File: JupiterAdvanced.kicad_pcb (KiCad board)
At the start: 2 copper layers, 314.8 x 162.9 mm, 224 parts, among them SW1 SW_Push, U1 PRTR5V0U2X, U10 ATmega32U4-AU, Y1 16MHz

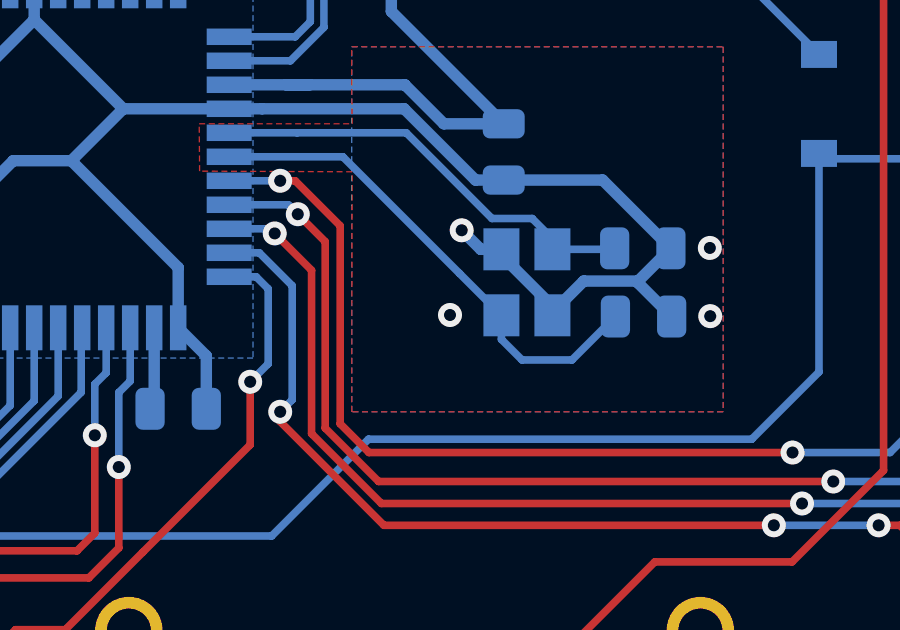
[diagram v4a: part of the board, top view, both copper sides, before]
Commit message: removed surplus via
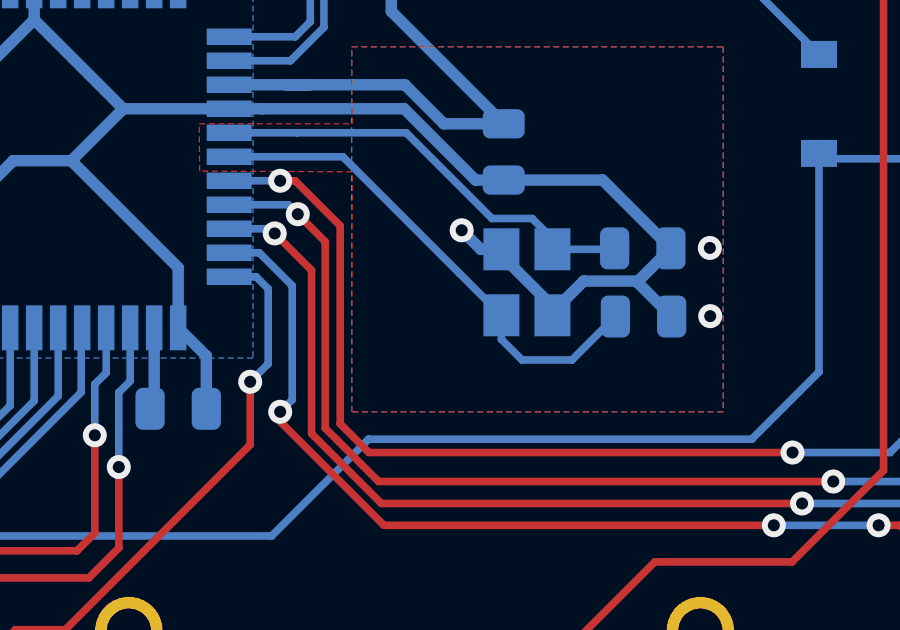
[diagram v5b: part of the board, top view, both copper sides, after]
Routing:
- net Net-(R7-Pad2): vias 1 -> 0
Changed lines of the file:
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@@
     (thickness 1.6)
     (drawings 547)
-    (tracks 996)
+    (tracks 995)
     (zones 0)
     (modules 224)
@@
   (segment (start 268.8625 98.905632) (end 265.725 102.043132) (width 0.254) (layer B.Cu) (net 139))
   (segment (start 268.8625 97.075) (end 268.8625 98.905632) (width 0.254) (layer B.Cu) (net 139))
-  (via (at 278.78532 113.74882) (size 0.8) (drill 0.4) (layers F.Cu B.Cu) (net 140))
   (segment (start 261.725 116.375) (end 261.325 116.775) (width 0.254) (layer B.Cu) (net 140))
   (segment (start 261.725 114.175) (end 261.725 116.375) (width 0.254) (layer B.Cu) (net 140))

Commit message: Rerouting for atmega32u4 complete
and its a complete mess...
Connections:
- U10 pad 10: ROW5 -> ROW6
- U10 pad 11: ROW6 -> ROW0
- U10 pad 9: ROW0 -> ROW5
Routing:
- net ROW5: track 586.8 -> 869.1 mm, vias 0 -> 2
- net ROW6: track 698.7 -> 832.7 mm, vias 0 -> 3
- net ROW0: track 517.7 -> 595.9 mm, vias 3 -> 8

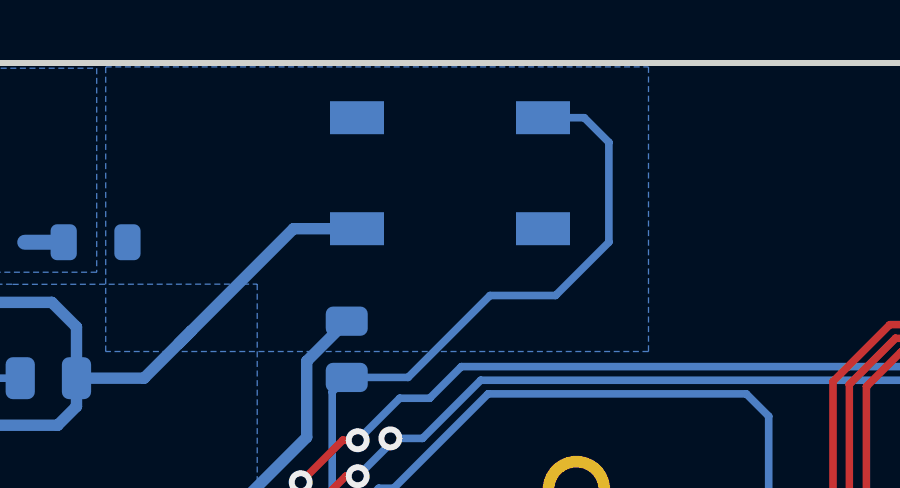
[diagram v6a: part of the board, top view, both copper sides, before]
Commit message: Push switch updated for JLCPCB
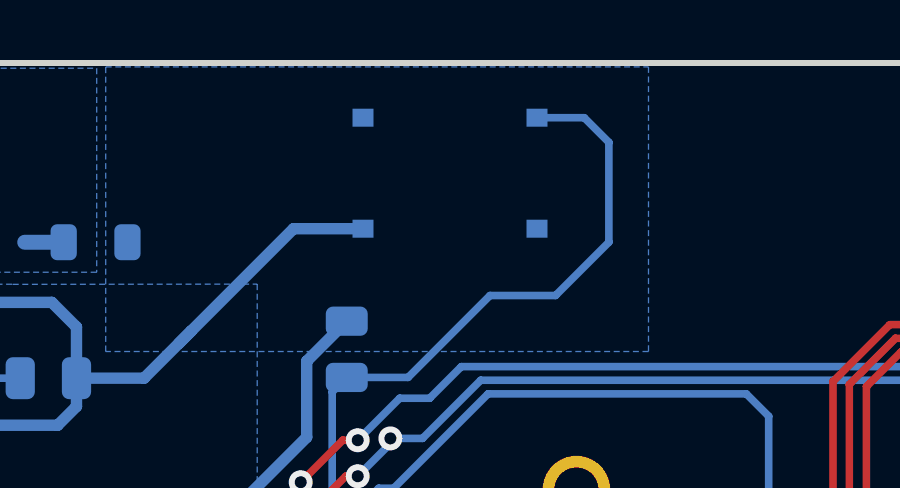
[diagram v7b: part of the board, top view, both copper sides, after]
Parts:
- SW1: footprint random-keyboard-parts:SKQG-1155865 -> JupiterAdvancedKbd_localFP:TS-1187A-B-A-B
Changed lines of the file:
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@@
     (add_net VCC)
+  )
+  (module JupiterAdvancedKbd_localFP:TS-1187A-B-A-B (layer B.Cu)
+    (at 283.00172 85.17382 180)
+    (fp_text reference SW1 (at 0.02794 3.556) (layer B.SilkS)
+      (effects (font (size 1 1) (thickness 0.15)) (justify mirror))
+    )
+    (fp_text value SW_Push (at -0.0254 -3.45948) (layer B.Fab)
+      (effects (font (size 1 1) (thickness 0.15)) (justify mirror))
+    )
+    (fp_line (start 3.25 2.15) (end 3.25 -2.15) (layer B.Fab) (width 0.12))
+    (fp_line (start -3.25 2.15) (end -3.25 -2.15) (layer B.Fab) (width 0.12))
+    (fp_line (start -3.25 -2.15) (end 3.25 -2.15) (layer B.Fab) (width 0.12))
+    (fp_line (start -3.25 2.15) (end 3.25 2.15) (layer B.Fab) (width 0.12))
+    (fp_line (start -3.2512 2.15392) (end -3.2512 -2.14608) (layer B.SilkS) (width 0.2))
+    (fp_line (start -3.2512 -2.15) (end 3.2488 -2.15) (layer B.SilkS) (width 0.2))
+    (fp_line (start 3.24612 2.15392) (end 3.24612 -2.14608) (layer B.SilkS) (width 0.2))
+    (fp_line (start -3.25388 2.15392) (end 3.24612 2.15392) (layer B.SilkS) (width 0.2))
+    (pad 1 smd rect (at -2.9 1.85 180) (size 0.7 0.6) (layers B.Cu B.Paste B.Mask)
+      (net 9 GND))
+    (pad 2 smd rect (at 2.9 1.85 180) (size 0.7 0.6) (layers B.Cu B.Paste B.Mask)
+      (net 131 "Net-(R8-Pad2)"))
+    (pad 3 smd rect (at -2.9 -1.85 180) (size 0.7 0.6) (layers B.Cu B.Paste B.Mask))
+    (pad 4 smd rect (at 2.9 -1.85 180) (size 0.7 0.6) (layers B.Cu B.Paste B.Mask))
   )
   (module Package_QFP:TQFP-44_10x10mm_P0.8mm (layer B.Cu)
@@
     (pad "" np_thru_hole circle (at 5.08 0 48.0996) (size 1.75 1.75) (drill 1.75) (layers *.Cu *.Mask))
   )
-  (module random-keyboard-parts:SKQG-1155865 (layer B.Cu)
-    (at 283.00172 85.17382 180)
-    (attr smd)
-    (fp_text reference SW1 (at 0 -4.064) (layer B.SilkS)
-      (effects (font (size 1 1) (thickness 0.15)) (justify mirror))
-    )
-    (fp_text value SW_Push (at 0 4.064) (layer B.Fab)
-      (effects (font (size 1 1) (thickness 0.15)) (justify mirror))
-    )
-    (fp_line (start -2.6 2.6) (end 2.6 2.6) (layer B.SilkS) (width 0.15))
-    (fp_line (start 2.6 2.6) (end 2.6 -2.6) (layer B.SilkS) (width 0.15))
-    (fp_line (start 2.6 -2.6) (end -2.6 -2.6) (layer B.SilkS) (width 0.15))
-    (fp_line (start -2.6 -2.6) (end -2.6 2.6) (layer B.SilkS) (width 0.15))
-    (fp_circle (center 0 0) (end 1 0) (layer B.SilkS) (width 0.15))
-    (fp_line (start -4.2 2.6) (end 4.2 2.6) (layer B.Fab) (width 0.15))
-    (fp_line (start 4.2 2.6) (end 4.2 1.2) (layer B.Fab) (width 0.15))
-    (fp_line (start 4.2 1.1) (end 2.6 1.1) (layer B.Fab) (width 0.15))
-    (fp_line (start 2.6 1.1) (end 2.6 -1.1) (layer B.Fab) (width 0.15))
-    (fp_line (start 2.6 -1.1) (end 4.2 -1.1) (layer B.Fab) (width 0.15))
-    (fp_line (start 4.2 -1.1) (end 4.2 -2.6) (layer B.Fab) (width 0.15))
-    (fp_line (start 4.2 -2.6) (end -4.2 -2.6) (layer B.Fab) (width 0.15))
-    (fp_line (start -4.2 -2.6) (end -4.2 -1.1) (layer B.Fab) (width 0.15))
-    (fp_line (start -4.2 -1.1) (end -2.6 -1.1) (layer B.Fab) (width 0.15))
-    (fp_line (start -2.6 -1.1) (end -2.6 1.1) (layer B.Fab) (width 0.15))
-    (fp_line (start -2.6 1.1) (end -4.2 1.1) (layer B.Fab) (width 0.15))
-    (fp_line (start -4.2 1.1) (end -4.2 2.6) (layer B.Fab) (width 0.15))
-    (fp_circle (center 0 0) (end 1 0) (layer B.Fab) (width 0.15))
-    (fp_line (start -2.6 1.1) (end -1.1 2.6) (layer B.Fab) (width 0.15))
-    (fp_line (start 2.6 1.1) (end 1.1 2.6) (layer B.Fab) (width 0.15))
-    (fp_line (start 2.6 -1.1) (end 1.1 -2.6) (layer B.Fab) (width 0.15))
-    (fp_line (start -2.6 -1.1) (end -1.1 -2.6) (layer B.Fab) (width 0.15))
-    (pad 4 smd rect (at -3.1 -1.85 180) (size 1.8 1.1) (layers B.Cu B.Paste B.Mask))
-    (pad 3 smd rect (at 3.1 1.85 180) (size 1.8 1.1) (layers B.Cu B.Paste B.Mask))
-    (pad 2 smd rect (at -3.1 1.85 180) (size 1.8 1.1) (layers B.Cu B.Paste B.Mask)
-      (net 131 "Net-(R8-Pad2)"))
-    (pad 1 smd rect (at 3.1 -1.85 180) (size 1.8 1.1) (layers B.Cu B.Paste B.Mask)
-      (net 9 GND))
-    (model ${KISYS3DMOD}/Button_Switch_SMD.3dshapes/SW_SPST_TL3342.step
-      (at (xyz 0 0 0))
-      (scale (xyz 1 1 1))
-      (rotate (xyz 0 0 0))
-    )
-  )
   (module MX_Only:MXOnly-6.25U-NoLED (layer F.Cu)

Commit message: JLCPCB Order SMT0210420181311
SMT0210420181311-3234210A
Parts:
- FB1: footprint Inductor_SMD:L_0805_2012Metric -> Inductor_SMD:L_1206_3216Metric
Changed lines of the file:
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@@
       (psa4output false)
       (plotreference true)
-      (plotvalue true)
+      (plotvalue false)
       (plotinvisibletext false)
       (padsonsilk false)
-      (subtractmaskfromsilk false)
+      (subtractmaskfromsilk true)
       (outputformat 1)
       (mirror false)
       (drillshape 0)
       (scaleselection 1)
-      (outputdirectory "Gerber/"))
+      (outputdirectory "JLCPCB/"))
   )
   (net 0 "")
@@
     (pad 4 smd rect (at 2.9 -1.85 180) (size 0.7 0.6) (layers B.Cu B.Paste B.Mask))
   )
+  (module Inductor_SMD:L_1206_3216Metric (layer B.Cu)
+    (at 271.1875 87.475 180)
+    (descr "Inductor SMD 1206 (3216 Metric), square (rectangular) end terminal, IPC_7351 nominal, (Body size source: IPC-SM-782 page 80, https://www.pcb-3d.com/wordpress/wp-content/uploads/ipc-sm-782a_amendment_1_and_2.pdf), generated with kicad-footprint-generator")
+    (tags inductor)
+    (attr smd)
+    (fp_text reference FB1 (at 0 1.9) (layer B.SilkS)
+      (effects (font (size 1 1) (thickness 0.15)) (justify mirror))
+    )
+    (fp_text value 60@100MHz (at 0 -1.9) (layer B.Fab)
+      (effects (font (size 1 1) (thickness 0.15)) (justify mirror))
+    )
+    (fp_text user %R (at 0 0) (layer B.Fab)
+      (effects (font (size 0.8 0.8) (thickness 0.12)) (justify mirror))
+    )
+    (fp_line (start -1.6 -0.8) (end -1.6 0.8) (layer B.Fab) (width 0.1))
+    (fp_line (start -1.6 0.8) (end 1.6 0.8) (layer B.Fab) (width 0.1))
+    (fp_line (start 1.6 0.8) (end 1.6 -0.8) (layer B.Fab) (width 0.1))
+    (fp_line (start 1.6 -0.8) (end -1.6 -0.8) (layer B.Fab) (width 0.1))
+    (fp_line (start -0.835242 0.91) (end 0.835242 0.91) (layer B.SilkS) (width 0.12))
+    (fp_line (start -0.835242 -0.91) (end 0.835242 -0.91) (layer B.SilkS) (width 0.12))
+    (fp_line (start -2.35 -1.2) (end -2.35 1.2) (layer B.CrtYd) (width 0.05))
+    (fp_line (start -2.35 1.2) (end 2.35 1.2) (layer B.CrtYd) (width 0.05))
+    (fp_line (start 2.35 1.2) (end 2.35 -1.2) (layer B.CrtYd) (width 0.05))
+    (fp_line (start 2.35 -1.2) (end -2.35 -1.2) (layer B.CrtYd) (width 0.05))
+    (pad 2 smd roundrect (at 1.575 0 180) (size 1.05 1.9) (layers B.Cu B.Paste B.Mask) (roundrect_rratio 0.2380942857142857)
+      (net 136 Earth))
+    (pad 1 smd roundrect (at -1.575 0 180) (size 1.05 1.9) (layers B.Cu B.Paste B.Mask) (roundrect_rratio 0.2380942857142857)
+      (net 9 GND))
+    (model ${KISYS3DMOD}/Inductor_SMD.3dshapes/L_1206_3216Metric.wrl
+      (at (xyz 0 0 0))
+      (scale (xyz 1 1 1))
+      (rotate (xyz 0 0 0))
+    )
+  )
   (module Package_QFP:TQFP-44_10x10mm_P0.8mm (layer B.Cu)
     (at 265.725 108.475 270)
@@
       (at (xyz 0 0 0))
       (scale (xyz 1 1 1))
-      (rotate (xyz 0 0 0))
-    )
-  )
-  (module Inductor_SMD:L_0805_2012Metric (layer B.Cu)
-    (at 271.1875 87.475 180)
-    (descr "Inductor SMD 0805 (2012 Metric), square (rectangular) end terminal, IPC_7351 nominal, (Body size source: IPC-SM-782 page 80, https://www.pcb-3d.com/wordpress/wp-content/uploads/ipc-sm-782a_amendment_1_and_2.pdf), generated with kicad-footprint-generator")
-    (tags inductor)
-    (attr smd)
-    (fp_text reference FB1 (at 0 1.55) (layer B.SilkS)
-      (effects (font (size 1 1) (thickness 0.15)) (justify mirror))
-    )
-    (fp_text value 60@100MHz (at 0 -1.55) (layer B.Fab)
-      (effects (font (size 1 1) (thickness 0.15)) (justify mirror))
-    )
-    (fp_line (start -1 -0.45) (end -1 0.45) (layer B.Fab) (width 0.1))
-    (fp_line (start -1 0.45) (end 1 0.45) (layer B.Fab) (width 0.1))
-    (fp_line (start 1 0.45) (end 1 -0.45) (layer B.Fab) (width 0.1))
-    (fp_line (start 1 -0.45) (end -1 -0.45) (layer B.Fab) (width 0.1))
-    (fp_line (start -0.399622 0.56) (end 0.399622 0.56) (layer B.SilkS) (width 0.12))
-    (fp_line (start -0.399622 -0.56) (end 0.399622 -0.56) (layer B.SilkS) (width 0.12))
-    (fp_line (start -1.75 -0.85) (end -1.75 0.85) (layer B.CrtYd) (width 0.05))
-    (fp_line (start -1.75 0.85) (end 1.75 0.85) (layer B.CrtYd) (width 0.05))
-    (fp_line (start 1.75 0.85) (end 1.75 -0.85) (layer B.CrtYd) (width 0.05))
-    (fp_line (start 1.75 -0.85) (end -1.75 -0.85) (layer B.CrtYd) (width 0.05))
-    (fp_text user %R (at 0 0) (layer B.Fab)
-      (effects (font (size 0.5 0.5) (thickness 0.08)) (justify mirror))
-    )
-    (pad 2 smd roundrect (at 1.0625 0 180) (size 0.875 1.2) (layers B.Cu B.Paste B.Mask) (roundrect_rratio 0.25)
-      (net 136 Earth))
-    (pad 1 smd roundrect (at -1.0625 0 180) (size 0.875 1.2) (layers B.Cu B.Paste B.Mask) (roundrect_rratio 0.25)
-      (net 9 GND))
-    (model ${KISYS3DMOD}/Inductor_SMD.3dshapes/L_0805_2012Metric.wrl
-      (at (xyz 0 0 0))
-      (scale (xyz 1 1 1))
